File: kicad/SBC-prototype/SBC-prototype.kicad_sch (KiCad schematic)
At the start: 0 parts

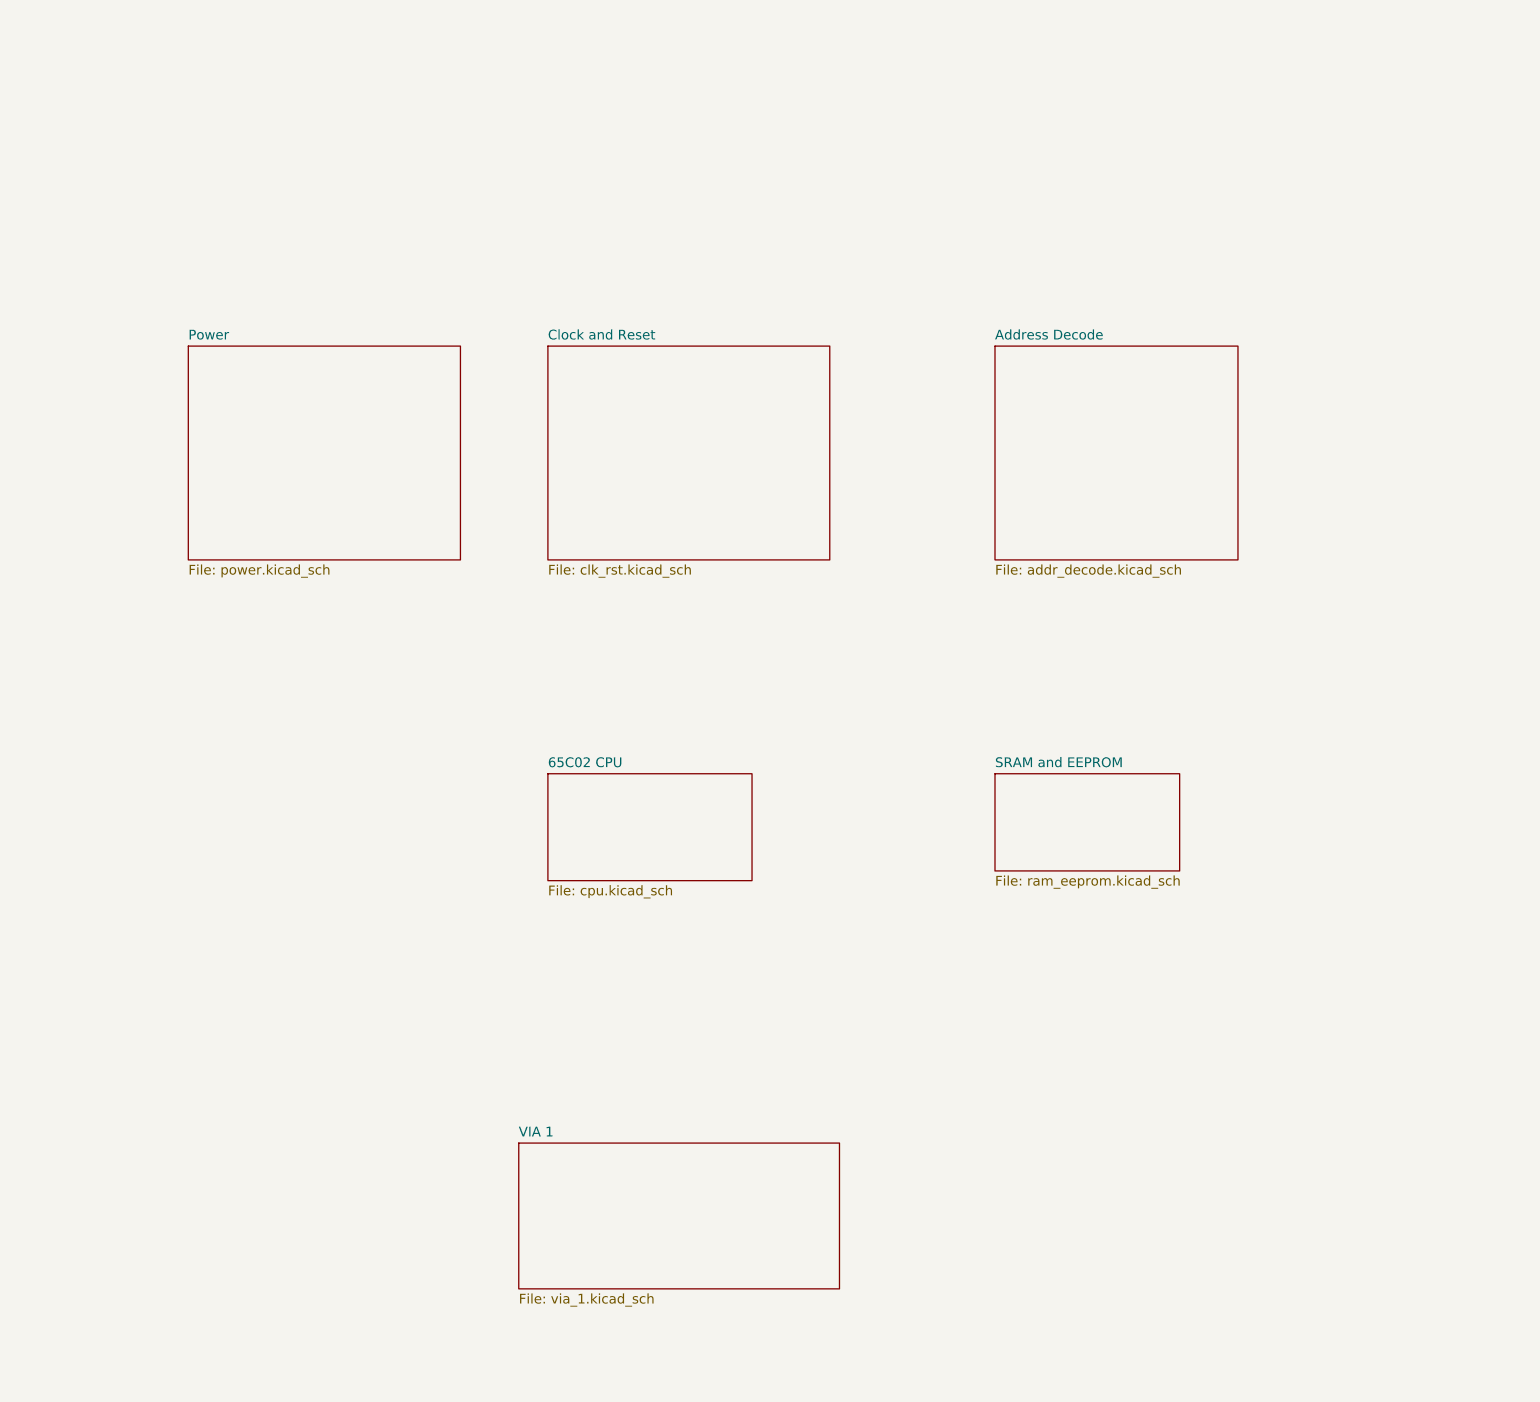
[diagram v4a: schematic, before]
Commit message: Started including hierarchical flow in the top level sheet
- First, hierarchical designs - I don't need a schematic to all fit on
  one sheet.
- I had the clock and reset lines as global labels, so I converted them
  to hierarchical labels instead, imported them on each sheet, and then
  connected the sheets together. It probably looks like overkill right
  now, but it will allow me to modify each block more easily
- The VIA has unconnected ports for now because I haven't wired them to
  anything on the prototyep in the lab yet. That's next, once the
  EEPROM, SRAM, and address decoders are all working (and VIA1 doesn't
  need a load except for maybe some resistors for now).
- Finally, the power rails and ground are global labels right now and
  aren't connected to anything on the top level design schematic. I'm
  not sure if that's normal, so for now I've just left them.
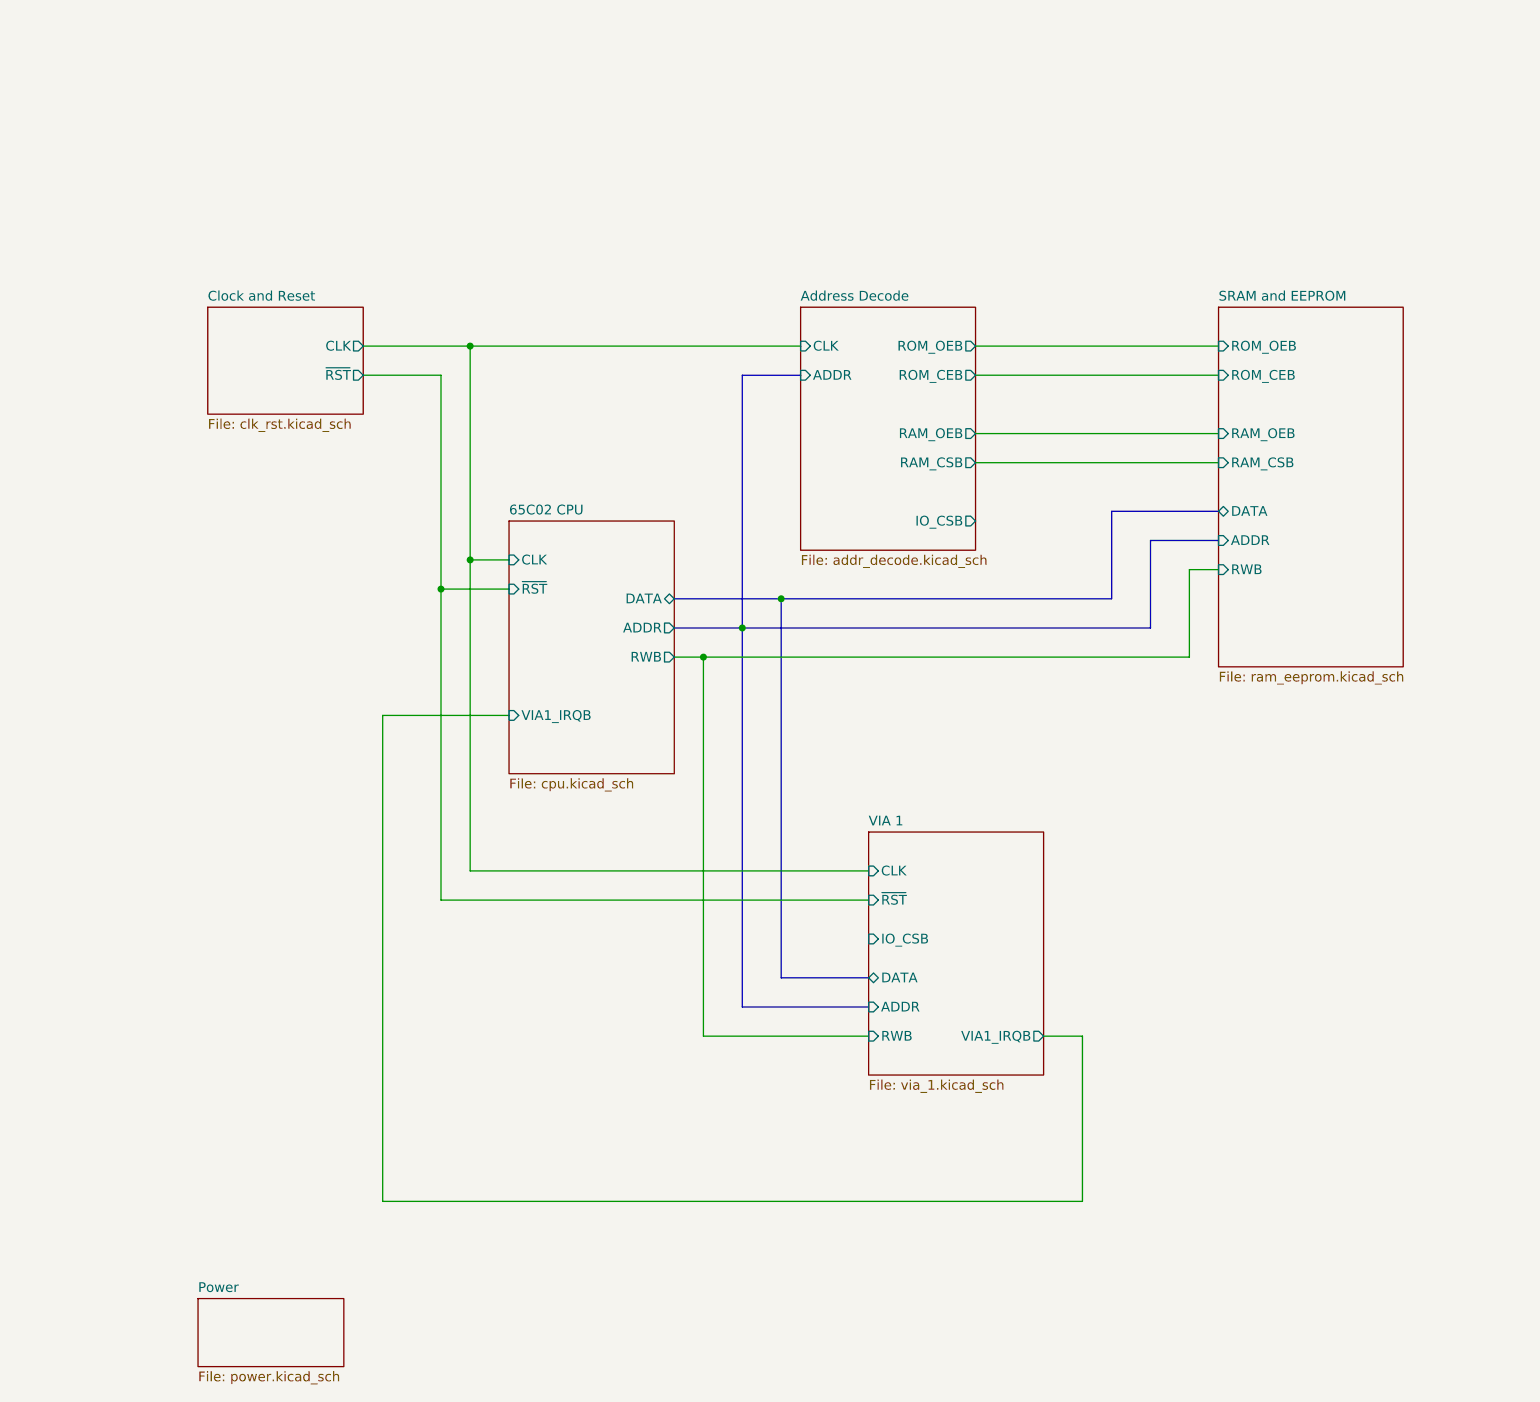
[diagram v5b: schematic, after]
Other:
- sheet 65C02 CPU ports: added ADDR, CLK, DATA, RWB, VIA1_IRQB, ~{RST}; removed none
- sheet Address Decode ports: added ADDR, CLK, IO_CSB, RAM_CSB, RAM_OEB, ROM_CEB, ROM_OEB; removed none
- sheet Clock and Reset ports: added CLK, ~{RST}; removed none
- sheet SRAM and EEPROM ports: added ADDR, DATA, RAM_CSB, RAM_OEB, ROM_CEB, ROM_OEB, RWB; removed none
- sheet VIA 1 ports: added ADDR, CLK, DATA, IO_CSB, RWB, VIA1_IRQB, ~{RST}; removed none

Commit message: Fixed a ton of DRC errors and warnings
- VIA 1 is still unconnected since it's on the breadboard that way and I
  haven't hooked it to anything yet
- All the parts in the library have changed because I've modified my own
  versions of them. I'm not sure if I should add my changes to the
  library or find a way to tell the tool that it's OK that those are
  updated.
- The 74HC00 NAND gate was completely broken and would have been an
  interesting problem to sort out during routing and placement
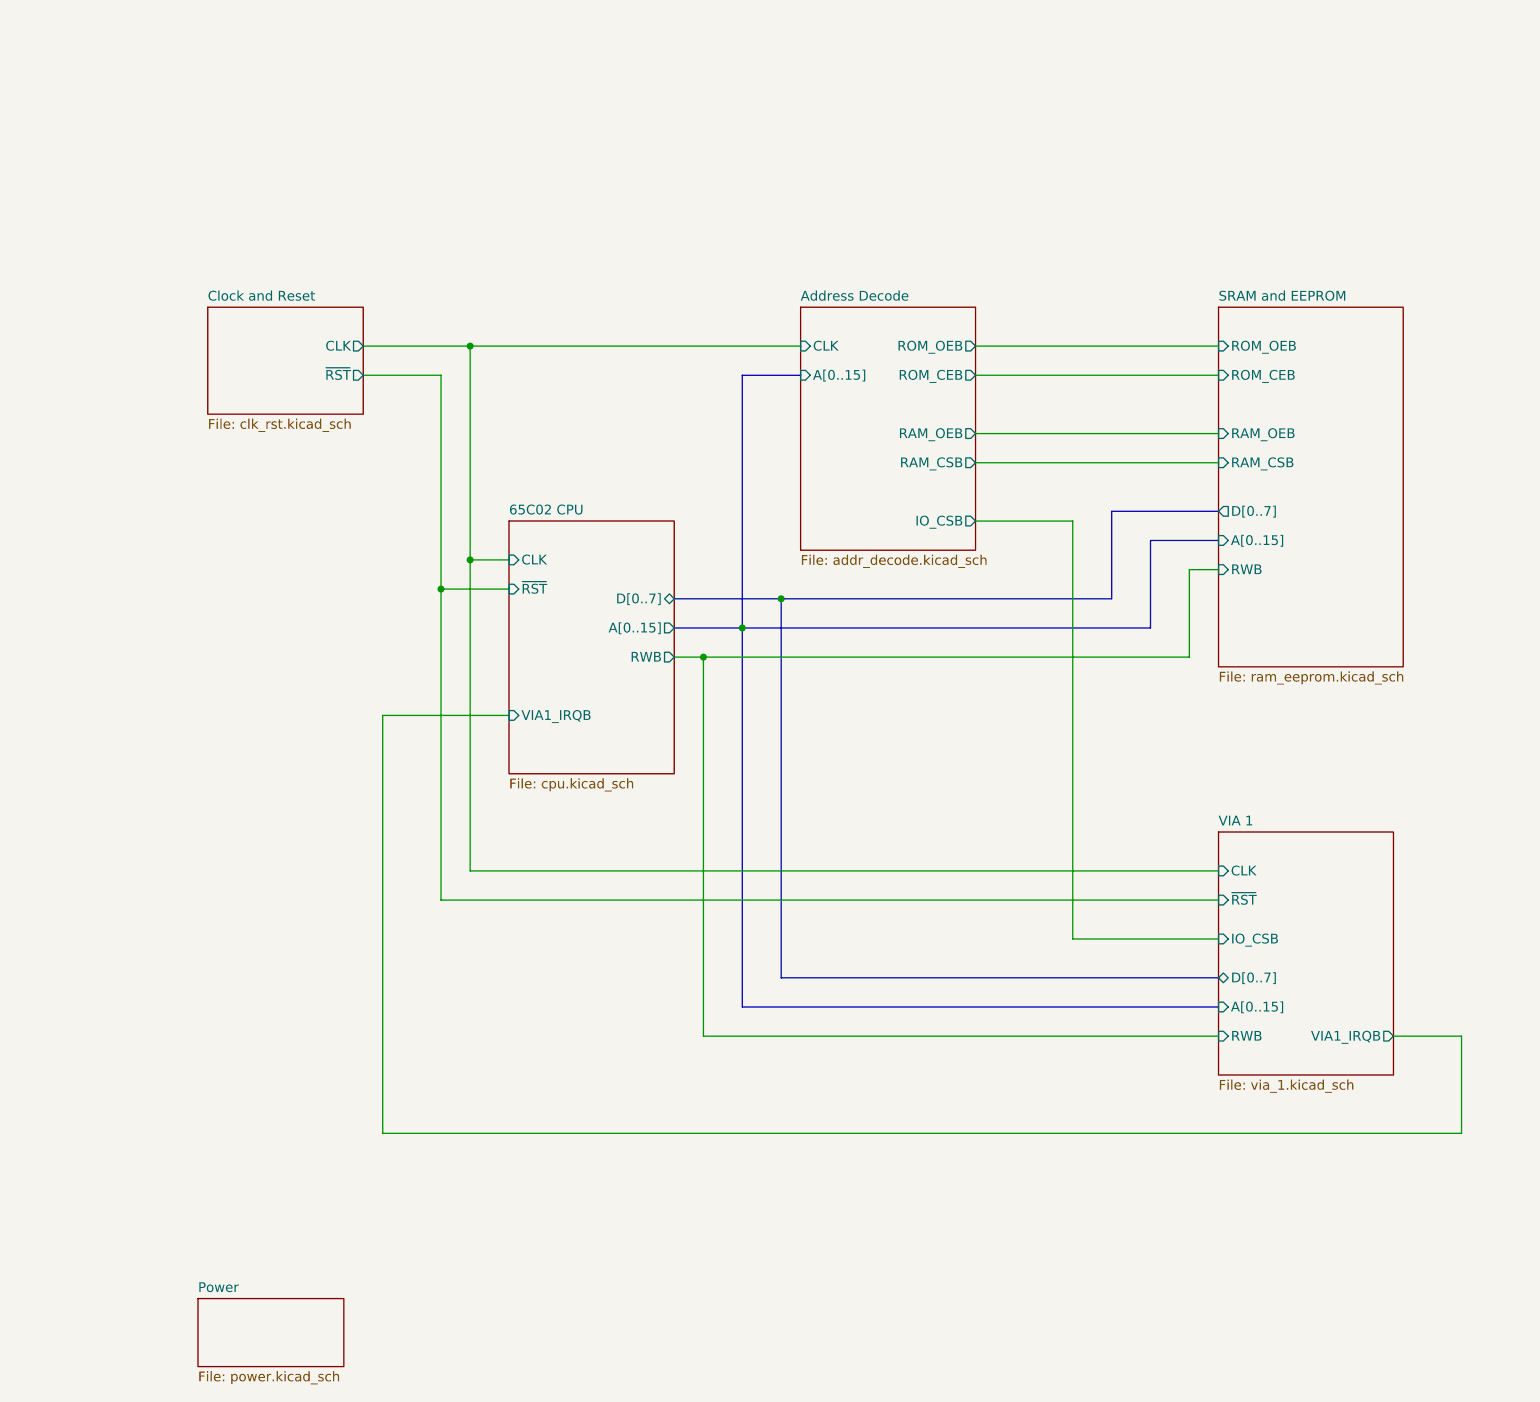
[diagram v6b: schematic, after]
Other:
- sheet 65C02 CPU ports: added A[0..15], D[0..7]; removed ADDR, DATA
- sheet Address Decode ports: added A[0..15]; removed ADDR
- sheet SRAM and EEPROM ports: added A[0..15], D[0..7]; removed ADDR, DATA
- sheet VIA 1 ports: added A[0..15], D[0..7]; removed ADDR, DATA
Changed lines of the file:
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@@
 	(wire
 		(pts
-			(xy 85.09 118.11) (xy 137.16 118.11)
+			(xy 163.83 72.39) (xy 163.83 127)
+		)
+		(stroke
+			(width 0)
+			(type default)
+		)
+	)
+	(wire
+		(pts
+			(xy 85.09 118.11) (xy 182.88 118.11)
 		)
 		(stroke
@@
 	(wire
 		(pts
-			(xy 73.66 161.29) (xy 165.1 161.29)
+			(xy 73.66 152.4) (xy 214.63 152.4)
 		)
 		(stroke
@@
 	(wire
 		(pts
-			(xy 73.66 161.29) (xy 73.66 97.79)
+			(xy 73.66 152.4) (xy 73.66 97.79)
 		)
 		(stroke
@@
 	(wire
 		(pts
-			(xy 165.1 139.7) (xy 165.1 161.29)
+			(xy 115.57 139.7) (xy 182.88 139.7)
 		)
 		(stroke
@@
 	(wire
 		(pts
+			(xy 205.74 139.7) (xy 214.63 139.7)
+		)
+		(stroke
+			(width 0)
+			(type default)
+		)
+	)
+	(wire
+		(pts
 			(xy 151.13 64.77) (xy 182.88 64.77)
 		)
@@
 	(wire
 		(pts
-			(xy 137.16 121.92) (xy 81.28 121.92)
+			(xy 182.88 121.92) (xy 81.28 121.92)
+		)
+		(stroke
+			(width 0)
+			(type default)
+		)
+	)
+	(wire
+		(pts
+			(xy 214.63 139.7) (xy 214.63 152.4)
 		)
 		(stroke
@@
 	(bus
 		(pts
-			(xy 125.73 132.08) (xy 137.16 132.08)
-		)
-		(stroke
-			(width 0)
-			(type default)
-		)
-	)
-	(wire
-		(pts
-			(xy 160.02 139.7) (xy 165.1 139.7)
+			(xy 125.73 132.08) (xy 182.88 132.08)
 		)
 		(stroke
@@
 	(wire
 		(pts
-			(xy 115.57 139.7) (xy 137.16 139.7)
-		)
-		(stroke
-			(width 0)
-			(type default)
-		)
-	)
-	(wire
-		(pts
 			(xy 115.57 90.17) (xy 179.07 90.17)
 		)
@@
 	(wire
 		(pts
+			(xy 163.83 127) (xy 182.88 127)
+		)
+		(stroke
+			(width 0)
+			(type default)
+		)
+	)
+	(wire
+		(pts
+			(xy 151.13 72.39) (xy 163.83 72.39)
+		)
+		(stroke
+			(width 0)
+			(type default)
+		)
+	)
+	(wire
+		(pts
 			(xy 73.66 97.79) (xy 90.17 97.79)
 		)
@@
 	(bus
 		(pts
-			(xy 120.65 135.89) (xy 137.16 135.89)
+			(xy 120.65 135.89) (xy 182.88 135.89)
 		)
 		(stroke
@@
 			)
 		)
-		(pin "DATA" bidirectional
-			(at 111.76 82.55 0)
-			(effects
-				(font
-					(size 1.27 1.27)
-				)
-				(justify right)
-			)
-		)
-		(pin "ADDR" output
-			(at 111.76 86.36 0)
-			(effects
-				(font
-					(size 1.27 1.27)
-				)
-				(justify right)
-			)
-		)
 		(pin "RWB" output
 			(at 111.76 90.17 0)
@@
 				)
 				(justify left)
+			)
+		)
+		(pin "A[0..15]" output
+			(at 111.76 86.36 0)
+			(effects
+				(font
+					(size 1.27 1.27)
+				)
+				(justify right)
+			)
+		)
+		(pin "D[0..7]" bidirectional
+			(at 111.76 82.55 0)
+			(effects
+				(font
+					(size 1.27 1.27)
+				)
+				(justify right)
 			)
 		)
@@
 			)
 		)
-		(pin "DATA" bidirectional
-			(at 182.88 71.12 180)
-			(effects
-				(font
-					(size 1.27 1.27)
-				)
-				(justify left)
-			)
-		)
 		(pin "RAM_CSB" input
 			(at 182.88 64.77 180)
@@
 			)
 		)
-		(pin "ADDR" input
-			(at 182.88 74.93 180)
-			(effects
-				(font
-					(size 1.27 1.27)
-				)
-				(justify left)
-			)
-		)
 		(pin "ROM_CEB" input
 			(at 182.88 53.34 180)
@@
 		(pin "ROM_OEB" input
 			(at 182.88 49.53 180)
+			(effects
+				(font
+					(size 1.27 1.27)
+				)
+				(justify left)
+			)
+		)
+		(pin "A[0..15]" input
+			(at 182.88 74.93 180)
+			(effects
+				(font
+					(size 1.27 1.27)
+				)
+				(justify left)
+			)
+		)
+		(pin "D[0..7]" output
+			(at 182.88 71.12 180)
 			(effects
 				(font
@@
 	)
 	(sheet
-		(at 137.16 113.03)
+		(at 182.88 113.03)
 		(size 22.86 31.75)
 		(fields_autoplaced yes)
@@
 		)
 		(property "Sheetname" "VIA 1"
-			(at 137.16 112.3184 0)
+			(at 182.88 112.3184 0)
 			(effects
 				(font
@@
 		)
 		(property "Sheetfile" "via_1.kicad_sch"
-			(at 137.16 145.3646 0)
+			(at 182.88 145.3646 0)
 			(effects
 				(font
@@
 		)
 		(pin "VIA1_IRQB" output
-			(at 160.02 139.7 0)
-			(effects
-				(font
-					(size 1.27 1.27)
-				)
-				(justify right)
-			)
-		)
-		(pin "DATA" bidirectional
-			(at 137.16 132.08 180)
-			(effects
-				(font
-					(size 1.27 1.27)
-				)
-				(justify left)
+			(at 205.74 139.7 0)
+			(effects
+				(font
+					(size 1.27 1.27)
+				)
+				(justify right)
 			)
 		)
 		(pin "IO_CSB" input
-			(at 137.16 127 180)
+			(at 182.88 127 180)
 			(effects
 				(font
@@
 		)
 		(pin "RWB" input
-			(at 137.16 139.7 180)
-			(effects
-				(font
-					(size 1.27 1.27)
-				)
-				(justify left)
-			)
-		)
-		(pin "ADDR" input
-			(at 137.16 135.89 180)
+			(at 182.88 139.7 180)
 			(effects
 				(font
@@
 		)
 		(pin "CLK" input
-			(at 137.16 118.11 180)
+			(at 182.88 118.11 180)
 			(effects
 				(font
@@
 		)
 		(pin "~{RST}" input
-			(at 137.16 121.92 180)
+			(at 182.88 121.92 180)
+			(effects
+				(font
+					(size 1.27 1.27)
+				)
+				(justify left)
+			)
+		)
+		(pin "A[0..15]" input
+			(at 182.88 135.89 180)
+			(effects
+				(font
+					(size 1.27 1.27)
+				)
+				(justify left)
+			)
+		)
+		(pin "D[0..7]" bidirectional
+			(at 182.88 132.08 180)
 			(effects
 				(font
@@
 			)
 		)
-		(pin "ADDR" input
-			(at 128.27 53.34 180)
-			(effects
-				(font
-					(size 1.27 1.27)
-				)
-				(justify left)
-			)
-		)
 		(pin "CLK" input
 			(at 128.27 49.53 180)
 			(effects
 				(font
+					(size 1.27 1.27)
+				)
+				(justify left)
+			)
+		)
+		(pin "A[0..15]" input
+			(at 128.27 53.34 180)
+			(effects
+				(font
